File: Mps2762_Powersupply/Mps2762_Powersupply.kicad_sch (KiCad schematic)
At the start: 53 parts, among them J1 124018312112A, J2 Conn_01x08_Pin, J3 Conn_01x02_Pin, J4 Conn_01x02_Pin, SW1 SW_DIP_x03, U1 MP2762AGV-0000-P, U2 CH224K, U3 AP62600SJ-7

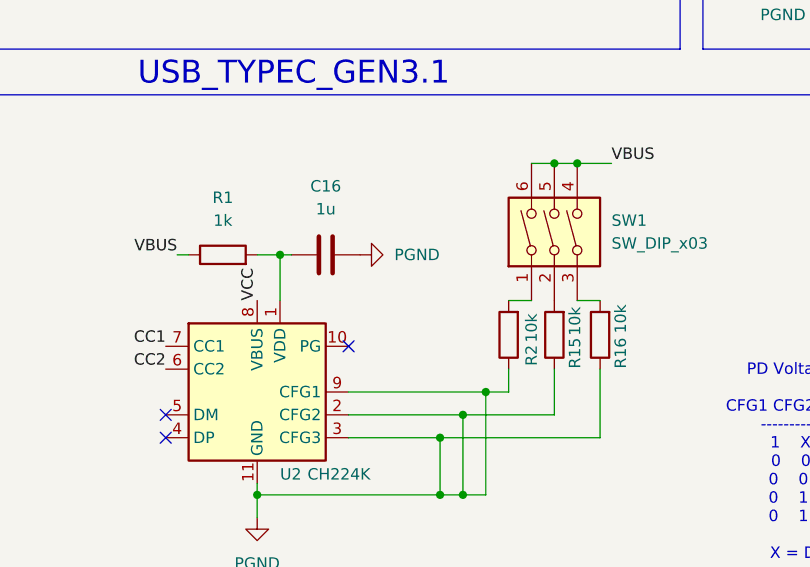
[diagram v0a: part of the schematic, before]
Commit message: added footprints
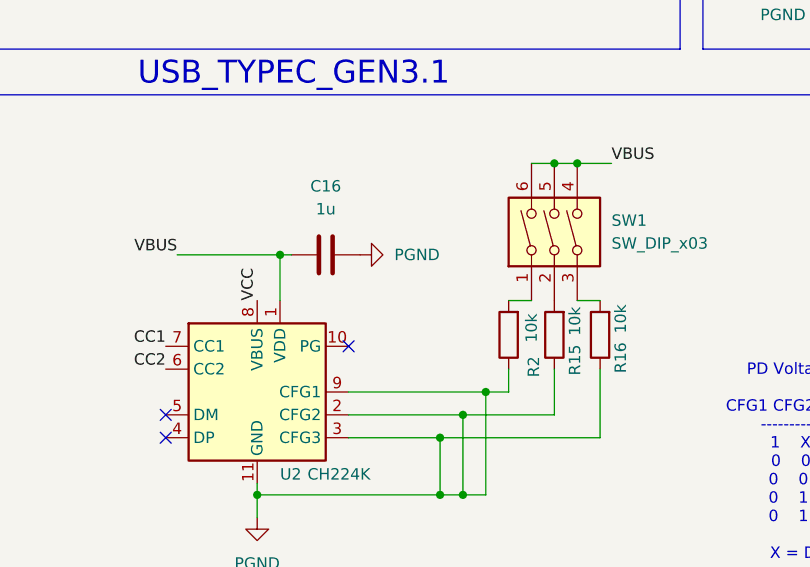
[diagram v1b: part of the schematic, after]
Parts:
- removed R1: 1k, symbol Device:R
- C1, C15, C2, C3, C4, C5, C6, C7: footprint (none) -> Capacitor_SMD:C_0805_2012Metric
- C10, C11, C12, C13, C14, C16, C17, C19, C20, C8, C9: footprint (none) -> Capacitor_SMD:C_0201_0603Metric
- C18: footprint (none) -> Capacitor_SMD:C_0402_1005Metric
- D1: footprint (none) -> LED_SMD:LED_0201_0603Metric
- J2: footprint (none) -> Connector_JST:JST_PH_B8B-PH-K_1x08_P2.00mm_Vertical
- J3, J4: footprint (none) -> Connector_Hirose:Hirose_DF13-02P-1.25DSA_1x02_P1.25mm_Vertical
- NT0: footprint (none) -> NetTie:NetTie-2_SMD_Pad0.5mm
- R10: footprint (none) -> Resistor_SMD:R_1206_3216Metric
- R11, R12, R13, R14, R15, R16, R17, R18, R19, R2, R20, R3, R6, R7, R8, R9: footprint (none) -> Resistor_SMD:R_0201_0603Metric
- R5: footprint (none) -> Resistor_SMD:R_0805_2012Metric
- U1: footprint QFN-30_MP2762A_MNP -> (none)
- U3: footprint AP62600SJ-7:IC_AP62600SJ-7 -> mps_footprints:IC_AP62600SJ-7
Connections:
- net VBUS: now also C16.2, U2.1 (VDD)
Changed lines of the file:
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@@
 	(wire
 		(pts
-			(xy 35.56 154.94) (xy 36.83 154.94)
+			(xy 35.56 154.94) (xy 46.99 154.94)
 		)
 		(stroke
@@
 	(wire
 		(pts
-			(xy 44.45 154.94) (xy 46.99 154.94)
-		)
-		(stroke
-			(width 0)
-			(type default)
-		)
-	)
-	(wire
-		(pts
 			(xy 67.31 172.72) (xy 67.31 181.61)
 		)
@@
 			)
 		)
-		(property "Footprint" ""
+		(property "Footprint" "Connector_JST:JST_PH_B8B-PH-K_1x08_P2.00mm_Vertical"
 			(at 160.02 125.73 0)
 			(hide yes)
@@
 			)
 		)
-		(property "Footprint" ""
+		(property "Footprint" "Capacitor_SMD:C_0805_2012Metric"
 			(at 130.5052 111.76 0)
 			(hide yes)
@@
 			)
 		)
-		(property "Footprint" ""
+		(property "Footprint" "Resistor_SMD:R_0201_0603Metric"
 			(at 101.092 67.31 90)
 			(hide yes)
@@
 			)
 		)
-		(property "Footprint" ""
+		(property "Footprint" "NetTie:NetTie-2_SMD_Pad0.5mm"
 			(at 203.2 76.2 0)
 			(hide yes)
@@
 			)
 		)
-		(property "Footprint" ""
+		(property "Footprint" "Capacitor_SMD:C_0201_0603Metric"
 			(at 191.77 51.1048 0)
 			(hide yes)
@@
 			)
 		)
-		(property "Footprint" ""
+		(property "Footprint" "Capacitor_SMD:C_0201_0603Metric"
 			(at 256.54 35.2552 0)
 			(hide yes)
@@
 			)
 		)
-		(property "Footprint" ""
+		(property "Footprint" "Capacitor_SMD:C_0402_1005Metric"
 			(at 237.49 55.5752 0)
 			(hide yes)
@@
 			)
 		)
-		(property "Footprint" ""
+		(property "Footprint" "Capacitor_SMD:C_0805_2012Metric"
 			(at 98.7552 121.92 0)
 			(hide yes)
@@
 			)
 		)
-		(property "Footprint" ""
+		(property "Footprint" "Capacitor_SMD:C_0201_0603Metric"
 			(at 196.5452 77.47 0)
 			(hide yes)
@@
 			)
 		)
-		(property "Footprint" ""
+		(property "Footprint" "Capacitor_SMD:C_0805_2012Metric"
 			(at 98.7552 111.76 0)
 			(hide yes)
@@
 			)
 		)
-		(property "Footprint" ""
+		(property "Footprint" "Resistor_SMD:R_0201_0603Metric"
 			(at 109.728 29.21 90)
 			(hide yes)
@@
 			)
 		)
-		(property "Footprint" ""
+		(property "Footprint" "Resistor_SMD:R_0201_0603Metric"
 			(at 118.872 29.21 90)
 			(hide yes)
@@
 			)
 		)
-		(property "Footprint" ""
+		(property "Footprint" "Capacitor_SMD:C_0201_0603Metric"
 			(at 190.5 122.2248 0)
 			(hide yes)
@@
 	(symbol
 		(lib_id "Device:R")
-		(at 40.64 154.94 90)
-		(unit 1)
-		(body_style 1)
-		(exclude_from_sim no)
-		(in_bom yes)
-		(on_board yes)
-		(in_pos_files yes)
-		(dnp no)
-		(fields_autoplaced yes)
-		(property "Reference" "R1"
-			(at 40.64 148.59 90)
-			(show_name no)
-			(do_not_autoplace no)
-			(effects
-				(font
-					(size 1.27 1.27)
-				)
-			)
-		)
-		(property "Value" "1k"
-			(at 40.64 151.13 90)
-			(show_name no)
-			(do_not_autoplace no)
-			(effects
-				(font
-					(size 1.27 1.27)
-				)
-			)
-		)
-		(property "Footprint" ""
-			(at 40.64 156.718 90)
-			(hide yes)
-			(show_name no)
-			(do_not_autoplace no)
-			(effects
-				(font
-					(size 1.27 1.27)
-				)
-			)
-		)
-		(property "Datasheet" ""
-			(at 40.64 154.94 0)
-			(hide yes)
-			(show_name no)
-			(do_not_autoplace no)
-			(effects
-				(font
-					(size 1.27 1.27)
-				)
-			)
-		)
-		(property "Description" "Resistor"
-			(at 40.64 154.94 0)
-			(hide yes)
-			(show_name no)
-			(do_not_autoplace no)
-			(effects
-				(font
-					(size 1.27 1.27)
-				)
-			)
-		)
-		(pin "1"
-		)
-		(pin "2"
-		)
-		(instances
-			(project "Mps2762_Powersupply"
-				(path "/f246fae6-c10e-4ee7-a5ca-45459b596580"
-					(reference "R1")
-					(unit 1)
-				)
-			)
-		)
-	)
-	(symbol
-		(lib_id "Device:R")
 		(at 260.35 43.18 270)
 		(unit 1)
@@
 			)
 		)
-		(property "Footprint" ""
+		(property "Footprint" "Resistor_SMD:R_0201_0603Metric"
 			(at 260.35 41.402 90)
 			(hide yes)
@@
 			)
 		)
-		(property "Footprint" ""
+		(property "Footprint" "Connector_Hirose:Hirose_DF13-02P-1.25DSA_1x02_P1.25mm_Vertical"
 			(at 198.12 100.33 0)
 			(hide yes)
@@
 			)
 		)
-		(property "Footprint" ""
+		(property "Footprint" "Resistor_SMD:R_0201_0603Metric"
 			(at 103.378 29.21 90)
 			(hide yes)
@@
 		(dnp no)
 		(property "Reference" "R15"
-			(at 79.756 165.862 90)
+			(at 79.756 166.624 90)
 			(show_name no)
 			(do_not_autoplace no)
@@
 			)
 		)
-		(property "Footprint" ""
+		(property "Footprint" "Resistor_SMD:R_0201_0603Metric"
 			(at 79.248 163.83 90)
 			(hide yes)
@@
 			)
 		)
-		(property "Footprint" ""
+		(property "Footprint" "Capacitor_SMD:C_0805_2012Metric"
 			(at 195.8848 26.67 0)
 			(hide yes)
@@
 			)
 		)
-		(property "Footprint" "AP62600SJ-7:IC_AP62600SJ-7"
+		(property "Footprint" "mps_footprints:IC_AP62600SJ-7"
 			(at 247.65 77.47 0)
 			(hide yes)
@@
 			)
 		)
-		(property "Footprint" ""
+		(property "Footprint" "Capacitor_SMD:C_0201_0603Metric"
 			(at 191.4652 77.47 0)
 			(hide yes)
@@
 			)
 		)
-		(property "Footprint" ""
+		(property "Footprint" "Capacitor_SMD:C_0201_0603Metric"
 			(at 203.2 124.1552 0)
 			(hide yes)
@@
 			)
 		)
-		(property "Footprint" "QFN-30_MP2762A_MNP"
+		(property "Footprint" ""
 			(at 116.84 57.15 0)
 			(hide yes)
@@
 			)
 		)
-		(property "Footprint" ""
+		(property "Footprint" "Resistor_SMD:R_0201_0603Metric"
 			(at 125.222 29.21 90)
 			(hide yes)
@@
 		(dnp no)
 		(property "Reference" "R16"
-			(at 84.836 165.862 90)
+			(at 84.836 166.37 90)
 			(show_name no)
 			(do_not_autoplace no)
@@
 			)
 		)
-		(property "Footprint" ""
+		(property "Footprint" "Resistor_SMD:R_0201_0603Metric"
 			(at 84.328 163.83 90)
 			(hide yes)
@@
 			)
 		)
-		(property "Footprint" ""
+		(property "Footprint" "Resistor_SMD:R_0201_0603Metric"
 			(at 260.35 47.752 90)
 			(hide yes)
@@
 			)
 		)
-		(property "Footprint" ""
+		(property "Footprint" "Capacitor_SMD:C_0201_0603Metric"
 			(at 190.5 114.6048 0)
 			(hide yes)
@@
 			)
 		)
-		(property "Footprint" ""
+		(property "Footprint" "Resistor_SMD:R_0201_0603Metric"
 			(at 101.092 57.15 90)
 			(hide yes)
@@
 			)
 		)
-		(property "Footprint" ""
+		(property "Footprint" "Capacitor_SMD:C_0805_2012Metric"
 			(at 120.3452 111.76 0)
 			(hide yes)
@@
 			)
 		)
-		(property "Footprint" ""
+		(property "Footprint" "Resistor_SMD:R_0805_2012Metric"
 			(at 185.42 71.628 90)
 			(hide yes)
@@
 			)
 		)
-		(property "Footprint" ""
+		(property "Footprint" "Capacitor_SMD:C_0201_0603Metric"
 			(at 227.33 55.5752 0)
 			(hide yes)
@@
 			)
 		)
-		(property "Footprint" ""
+		(property "Footprint" "Capacitor_SMD:C_0201_0603Metric"
 			(at 48.26 155.9052 0)
 			(hide yes)
@@
 			)
 		)
-		(property "Footprint" ""
+		(property "Footprint" "LED_SMD:LED_0201_0603Metric"
 			(at 133.35 29.21 0)
 			(hide yes)
@@
 			)
 		)
-		(property "Footprint" ""
+		(property "Footprint" "Capacitor_SMD:C_0201_0603Metric"
 			(at 180.6448 26.67 0)
 			(hide yes)
@@
 			)
 		)
-		(property "Footprint" ""
+		(property "Footprint" "Resistor_SMD:R_0201_0603Metric"
 			(at 182.372 41.91 90)
 			(hide yes)
@@
 			)
 		)
-		(property "Footprint" ""
+		(property "Footprint" "Capacitor_SMD:C_0201_0603Metric"
 			(at 240.03 108.9152 0)
 			(hide yes)
@@
 			)
 		)
-		(property "Footprint" ""
+		(property "Footprint" "Connector_Hirose:Hirose_DF13-02P-1.25DSA_1x02_P1.25mm_Vertical"
 			(at 259.08 115.57 0)
 			(hide yes)
@@
 			)
 		)
-		(property "Footprint" ""
+		(property "Footprint" "Resistor_SMD:R_1206_3216Metric"
 			(at 187.96 36.068 90)
 			(hide yes)
@@
 		(dnp no)
 		(property "Reference" "R2"
-			(at 74.93 166.116 90)
+			(at 75.184 167.386 90)
 			(show_name no)
 			(do_not_autoplace no)
@@
 			)
 		)
-		(property "Footprint" ""
+		(property "Footprint" "Resistor_SMD:R_0201_0603Metric"
 			(at 74.168 163.83 90)
 			(hide yes)
@@
 			)
 		)
-		(property "Footprint" ""
+		(property "Footprint" "Resistor_SMD:R_0201_0603Metric"
 			(at 112.522 29.21 90)
 			(hide yes)
@@
 			)
 		)
-		(property "Footprint" ""
+		(property "Footprint" "Resistor_SMD:R_0201_0603Metric"
 			(at 189.992 41.91 90)
 			(hide yes)
@@
 			)
 		)
-		(property "Footprint" ""
+		(property "Footprint" "Capacitor_SMD:C_0805_2012Metric"
 			(at 109.8402 111.6623 0)
 			(hide yes)
@@
 			)
 		)
-		(property "Footprint" ""
+		(property "Footprint" "Capacitor_SMD:C_0805_2012Metric"
 			(at 140.6652 111.76 0)
 			(hide yes)
@@
 			)
 		)
-		(property "Footprint" ""
+		(property "Footprint" "Resistor_SMD:R_0201_0603Metric"
 			(at 250.19 41.402 90)
 			(hide yes)
@@
 			)
 		)
-		(property "Footprint" ""
+		(property "Footprint" "Capacitor_SMD:C_0805_2012Metric"
 			(at 108.9152 121.92 0)
 			(hide yes)
@@
 			)
 		)
-		(property "Footprint" ""
+		(property "Footprint" "Resistor_SMD:R_0201_0603Metric"
 			(at 244.348 99.06 90)
 			(hide yes)
